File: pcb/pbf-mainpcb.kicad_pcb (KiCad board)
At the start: 2 copper layers, 42.5 x 76 mm, 66 parts, among them J1 USB_B_Micro, J2 Conn_01x02_Female, J3 Conn_01x02_Female, J4 Conn_01x03_Female, J5 Conn_01x05_Female, J6 Conn_01x04_Female, J7 Conn_01x10_Female, Q1 AO3401, SW1 SW_SPDT, U1 TCA9534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

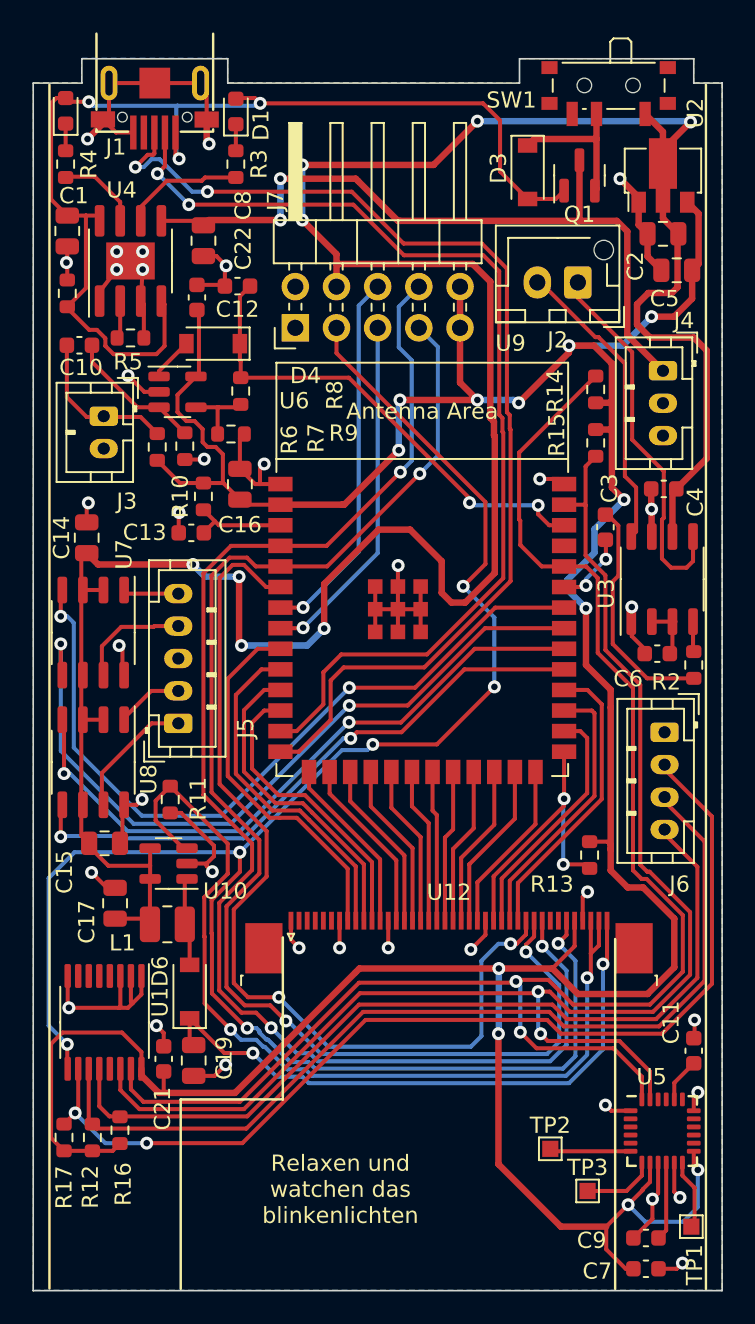
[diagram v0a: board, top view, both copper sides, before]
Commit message: Fix things I bodged in my prototype
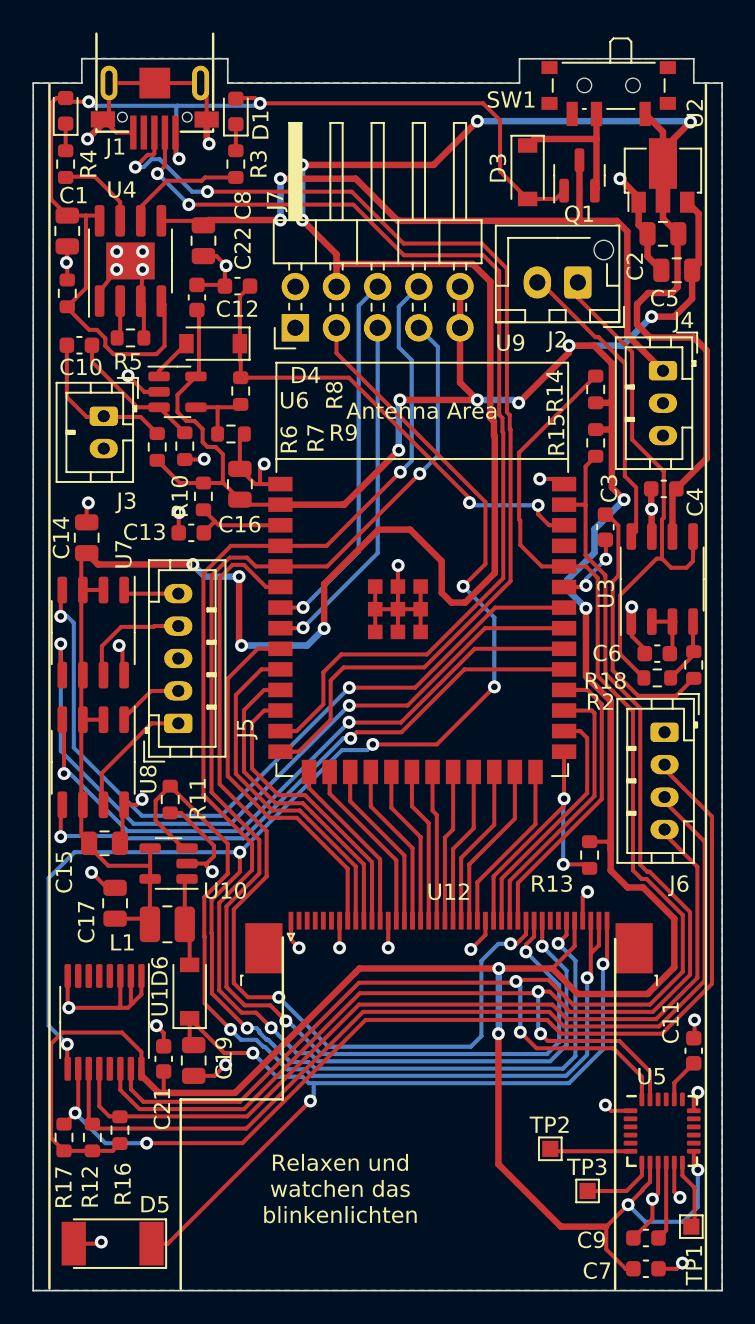
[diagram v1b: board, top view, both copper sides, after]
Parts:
- added D5: 12V zener, Diode_SMD:D_MELF, F.Cu at (154.9, 111.6)
- added R18: 10K, Resistor_SMD:R_0603_1608Metric, F.Cu at (188.5, 76.7)
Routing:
- net MLCD_A: track 37.7 -> 52.3 mm, vias 2 -> 3
- net Net-(J2-Pad1): track 23.1 -> 32.4 mm
- net Net-(U3-Pad4): track 1.87 -> 4.08 mm
- net Net-(C3-Pad1): track 14.4 -> 16.3 mm
- net GND: track 123.6 -> 125.3 mm, vias 36 -> 37
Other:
- board text added: "Pinball Fantasies playfield board v1.1a (C) 2022 Spritesmods.com"
- board text removed: "Pinball Fantasies playfield board v1.1 (C) 2022 Spritesmods.com"
